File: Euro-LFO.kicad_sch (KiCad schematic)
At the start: 40 parts, among them J1 2×5 2.54 mm shrouded IDC box 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, J3 Conn_01x07_Socket, J4 Conn_01x07_Pin, J5 Conn_01x07_Socket, J6 Conn_01x07_Pin, Q1 MMBT3904, U1 TL074CDR

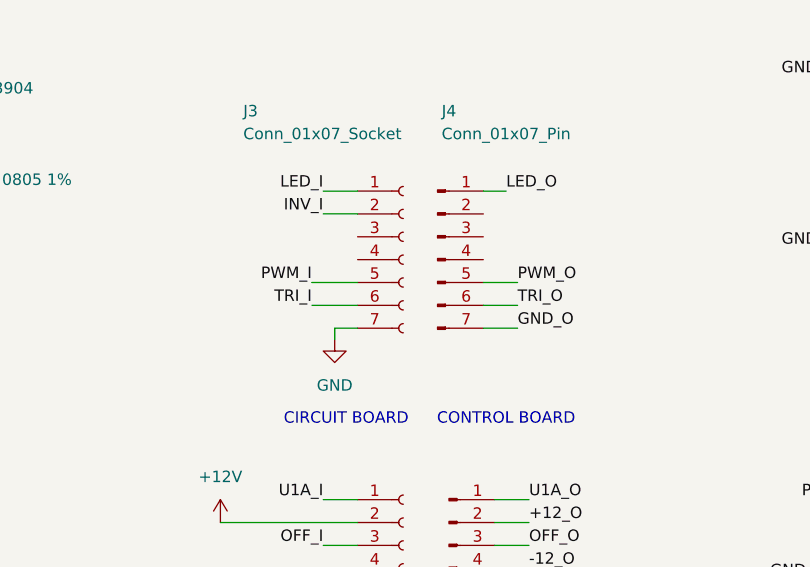
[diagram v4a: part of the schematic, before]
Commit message: flipped parts
Flipped parts, cleaned up edge cuts, untangled rats nest.
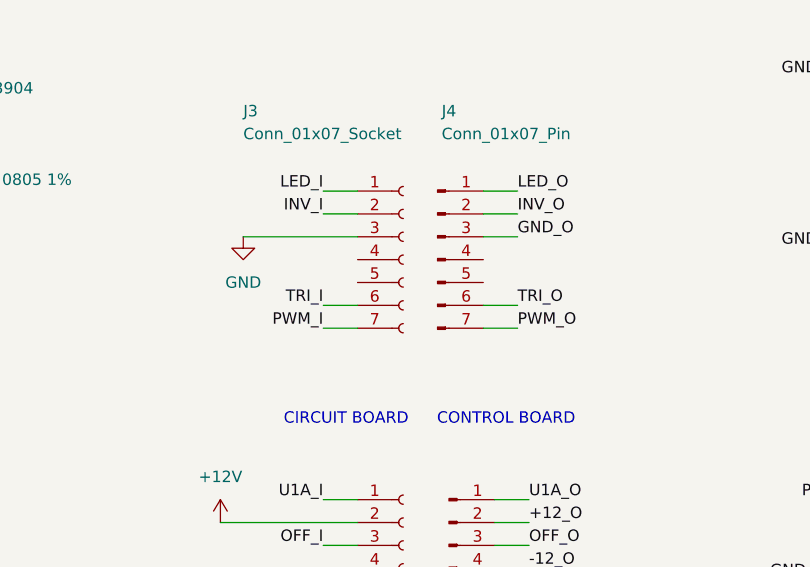
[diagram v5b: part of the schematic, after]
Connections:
- net GND: now also J3.3 (Pin_3); no longer J3.7 (Pin_7)
- net GND_O: now also J4.3 (Pin_3); no longer J4.7 (Pin_7)
- net PWM_I: now also J3.7 (Pin_7); no longer J3.5 (Pin_5)
- net PWM_O: now also J4.7 (Pin_7); no longer J4.5 (Pin_5)
- net INV_O: now reaches J4.2 (Pin_2)
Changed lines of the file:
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@@
 	(wire
 		(pts
+			(xy 194.31 59.69) (xy 198.12 59.69)
+		)
+		(stroke
+			(width 0)
+			(type default)
+		)
+	)
+	(wire
+		(pts
 			(xy 68.58 185.42) (xy 69.85 185.42)
 		)
@@
 	(wire
 		(pts
-			(xy 198.12 62.23) (xy 195.58 62.23)
+			(xy 143.51 109.22) (xy 143.51 116.84)
 		)
 		(stroke
@@
 	(wire
 		(pts
-			(xy 143.51 109.22) (xy 143.51 116.84)
+			(xy 106.68 64.77) (xy 107.95 64.77)
 		)
 		(stroke
@@
 	(wire
 		(pts
-			(xy 106.68 64.77) (xy 107.95 64.77)
+			(xy 90.17 64.77) (xy 90.17 67.31)
 		)
 		(stroke
@@
 	(wire
 		(pts
-			(xy 90.17 64.77) (xy 90.17 67.31)
+			(xy 110.49 99.06) (xy 111.76 99.06)
 		)
 		(stroke
@@
 	(wire
 		(pts
-			(xy 110.49 99.06) (xy 111.76 99.06)
+			(xy 102.87 172.72) (xy 107.95 172.72)
 		)
 		(stroke
@@
 	(wire
 		(pts
-			(xy 102.87 172.72) (xy 107.95 172.72)
+			(xy 119.38 66.04) (xy 118.11 66.04)
 		)
 		(stroke
@@
 	(wire
 		(pts
-			(xy 119.38 66.04) (xy 118.11 66.04)
+			(xy 212.09 62.23) (xy 215.9 62.23)
 		)
 		(stroke
@@
 	(wire
 		(pts
-			(xy 115.57 109.22) (xy 115.57 106.68)
+			(xy 215.9 52.07) (xy 212.09 52.07)
 		)
 		(stroke
@@
 	(wire
 		(pts
-			(xy 142.24 109.22) (xy 143.51 109.22)
+			(xy 115.57 109.22) (xy 115.57 106.68)
 		)
 		(stroke
@@
 	(wire
 		(pts
-			(xy 195.58 62.23) (xy 195.58 63.5)
+			(xy 142.24 109.22) (xy 143.51 109.22)
 		)
 		(stroke
@@
 	(wire
 		(pts
+			(xy 212.09 49.53) (xy 215.9 49.53)
+		)
+		(stroke
+			(width 0)
+			(type default)
+		)
+	)
+	(wire
+		(pts
 			(xy 125.73 106.68) (xy 125.73 97.79)
 		)
@@
 	(wire
 		(pts
-			(xy 193.04 57.15) (xy 198.12 57.15)
-		)
-		(stroke
-			(width 0)
-			(type default)
-		)
-	)
-	(wire
-		(pts
 			(xy 107.95 181.61) (xy 107.95 184.15)
 		)
@@
 	(wire
 		(pts
-			(xy 193.04 59.69) (xy 198.12 59.69)
+			(xy 194.31 62.23) (xy 198.12 62.23)
+		)
+		(stroke
+			(width 0)
+			(type default)
+		)
+	)
+	(wire
+		(pts
+			(xy 185.42 52.07) (xy 198.12 52.07)
 		)
 		(stroke
@@
 	(wire
 		(pts
-			(xy 212.09 46.99) (xy 214.63 46.99)
+			(xy 212.09 46.99) (xy 215.9 46.99)
 		)
 		(stroke
@@
 	(wire
 		(pts
-			(xy 212.09 59.69) (xy 215.9 59.69)
-		)
-		(stroke
-			(width 0)
-			(type default)
-		)
-	)
-	(wire
-		(pts
 			(xy 261.62 140.97) (xy 261.62 143.51)
 		)
@@
 	(wire
 		(pts
-			(xy 212.09 62.23) (xy 215.9 62.23)
-		)
-		(stroke
-			(width 0)
-			(type default)
-		)
-	)
-	(wire
-		(pts
 			(xy 213.36 88.9) (xy 217.17 88.9)
 		)
@@
 	(wire
 		(pts
-			(xy 212.09 57.15) (xy 215.9 57.15)
+			(xy 134.62 53.34) (xy 134.62 34.29)
 		)
 		(stroke
@@
 	(wire
 		(pts
-			(xy 134.62 53.34) (xy 134.62 34.29)
+			(xy 251.46 43.18) (xy 252.73 43.18)
 		)
 		(stroke
@@
 	(wire
 		(pts
-			(xy 251.46 43.18) (xy 252.73 43.18)
+			(xy 254 29.21) (xy 251.46 29.21)
 		)
 		(stroke
@@
 	(wire
 		(pts
-			(xy 254 29.21) (xy 251.46 29.21)
+			(xy 87.63 55.88) (xy 90.17 55.88)
 		)
 		(stroke
@@
 	(wire
 		(pts
-			(xy 87.63 55.88) (xy 90.17 55.88)
+			(xy 212.09 59.69) (xy 215.9 59.69)
 		)
 		(stroke
@@
 	)
 	(label "GND_O"
-		(at 215.9 62.23 0)
+		(at 215.9 52.07 0)
 		(effects
 			(font
@@
 	)
 	(label "TRI_I"
-		(at 193.04 59.69 180)
+		(at 194.31 59.69 180)
 		(effects
 			(font
@@
 	)
 	(label "PWM_O"
-		(at 215.9 57.15 0)
+		(at 215.9 62.23 0)
 		(effects
 			(font
@@
 	)
 	(label "LED_O"
-		(at 214.63 46.99 0)
+		(at 215.9 46.99 0)
 		(effects
 			(font
@@
 		)
 	)
+	(label "INV_O"
+		(at 215.9 49.53 0)
+		(effects
+			(font
+				(size 1.27 1.27)
+			)
+			(justify left bottom)
+		)
+	)
 	(label "U1A_I"
 		(at 194.31 81.28 180)
@@
 	)
 	(label "PWM_I"
-		(at 193.04 57.15 180)
+		(at 194.31 62.23 180)
 		(effects
 			(font
@@
 	(symbol
 		(lib_id "power:GND")
-		(at 195.58 63.5 0)
+		(at 185.42 52.07 0)
 		(mirror y)
 		(unit 1)
@@
 		(fields_autoplaced yes)
 		(property "Reference" "#PWR011"
-			(at 195.58 69.85 0)
+			(at 185.42 58.42 0)
 			(hide yes)
 			(show_name no)
@@
 		)
 		(property "Value" "GND"
-			(at 195.58 68.58 0)
+			(at 185.42 57.15 0)
 			(show_name no)
 			(do_not_autoplace no)
@@
 		)
 		(property "Footprint" ""
-			(at 195.58 63.5 0)
+			(at 185.42 52.07 0)
 			(hide yes)
 			(show_name no)
@@
 		)
 		(property "Datasheet" ""
-			(at 195.58 63.5 0)
+			(at 185.42 52.07 0)
 			(hide yes)
 			(show_name no)
@@
 		)
 		(property "Description" "Power symbol creates a global label with name \"GND\" , ground"
-			(at 195.58 63.5 0)
+			(at 185.42 52.07 0)
 			(hide yes)
 			(show_name no)

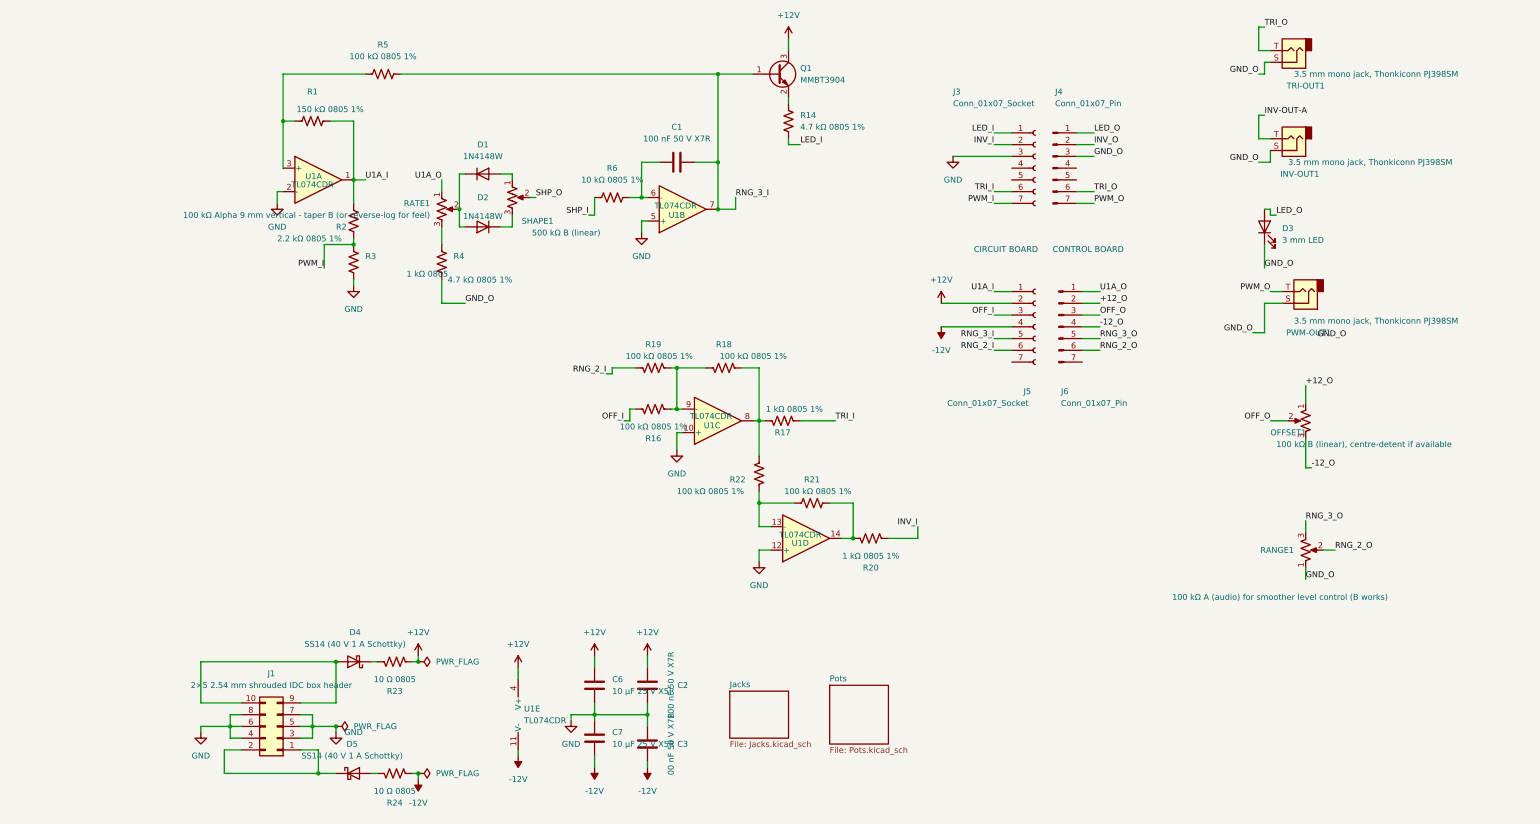
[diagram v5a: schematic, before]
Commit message: added mousebites
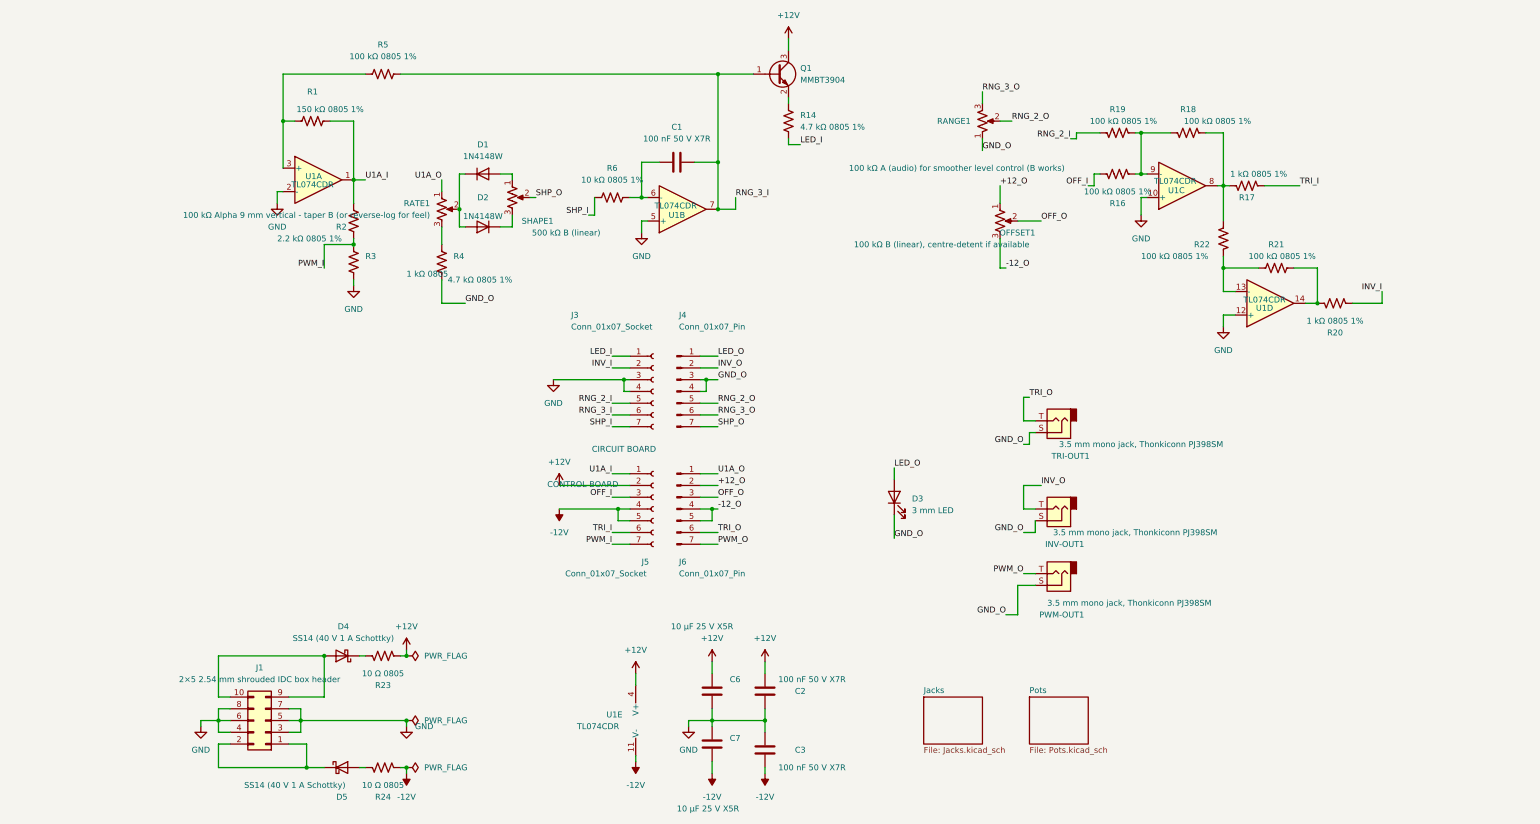
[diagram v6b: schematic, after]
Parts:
- C3: value 00 nF 50 V X7R -> 100 nF 50 V X7R
- J3, J5: footprint Connector_PinHeader_2.54mm:PinHeader_1x07_P2.54mm_Vertical -> Connector_PinSocket_2.54mm:PinSocket_1x07_P2.54mm_Vertical
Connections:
- net INV-OUT-A is gone; now on net INV_O: INV-OUT1.T
- net -12V: now also J5.5 (Pin_5)
- net -12_O: now also J6.5 (Pin_5)
- net GND: now also J3.4 (Pin_4)
- net GND_O: now also J4.4 (Pin_4)
- net PWM_I: now also J5.7 (Pin_7); no longer J3.7 (Pin_7)
- net PWM_O: now also J6.7 (Pin_7); no longer J4.7 (Pin_7)
- net RNG_2_I: now also J3.5 (Pin_5); no longer J5.6 (Pin_6)
- net RNG_2_O: now also J4.5 (Pin_5); no longer J6.6 (Pin_6)
- net RNG_3_I: now also J3.6 (Pin_6); no longer J5.5 (Pin_5)
- net RNG_3_O: now also J4.6 (Pin_6); no longer J6.5 (Pin_5)
- net SHP_I: now also J3.7 (Pin_7)
- net SHP_O: now also J4.7 (Pin_7)
- net TRI_I: now also J5.6 (Pin_6); no longer J3.6 (Pin_6)
- net TRI_O: now also J6.6 (Pin_6); no longer J4.6 (Pin_6)
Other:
- moved on the sheet: C2, C3, C6, C7, D3, D4, D5, INV-OUT1, J1, J3, J4, J5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
